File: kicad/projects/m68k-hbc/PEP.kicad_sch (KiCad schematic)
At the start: 10 parts, among them J1 PEP_Power_DIN41612_3x10, J12 PEP_Power_DIN41612_3x10, J13 PEP_Data_DIN41612_3x32, J2 PEP_Data_DIN41612_3x32, J5 PEP_Power_DIN41612_3x10, J8 PEP_Data_DIN41612_3x32, U13 74LS02, U23 MCP23017_SO

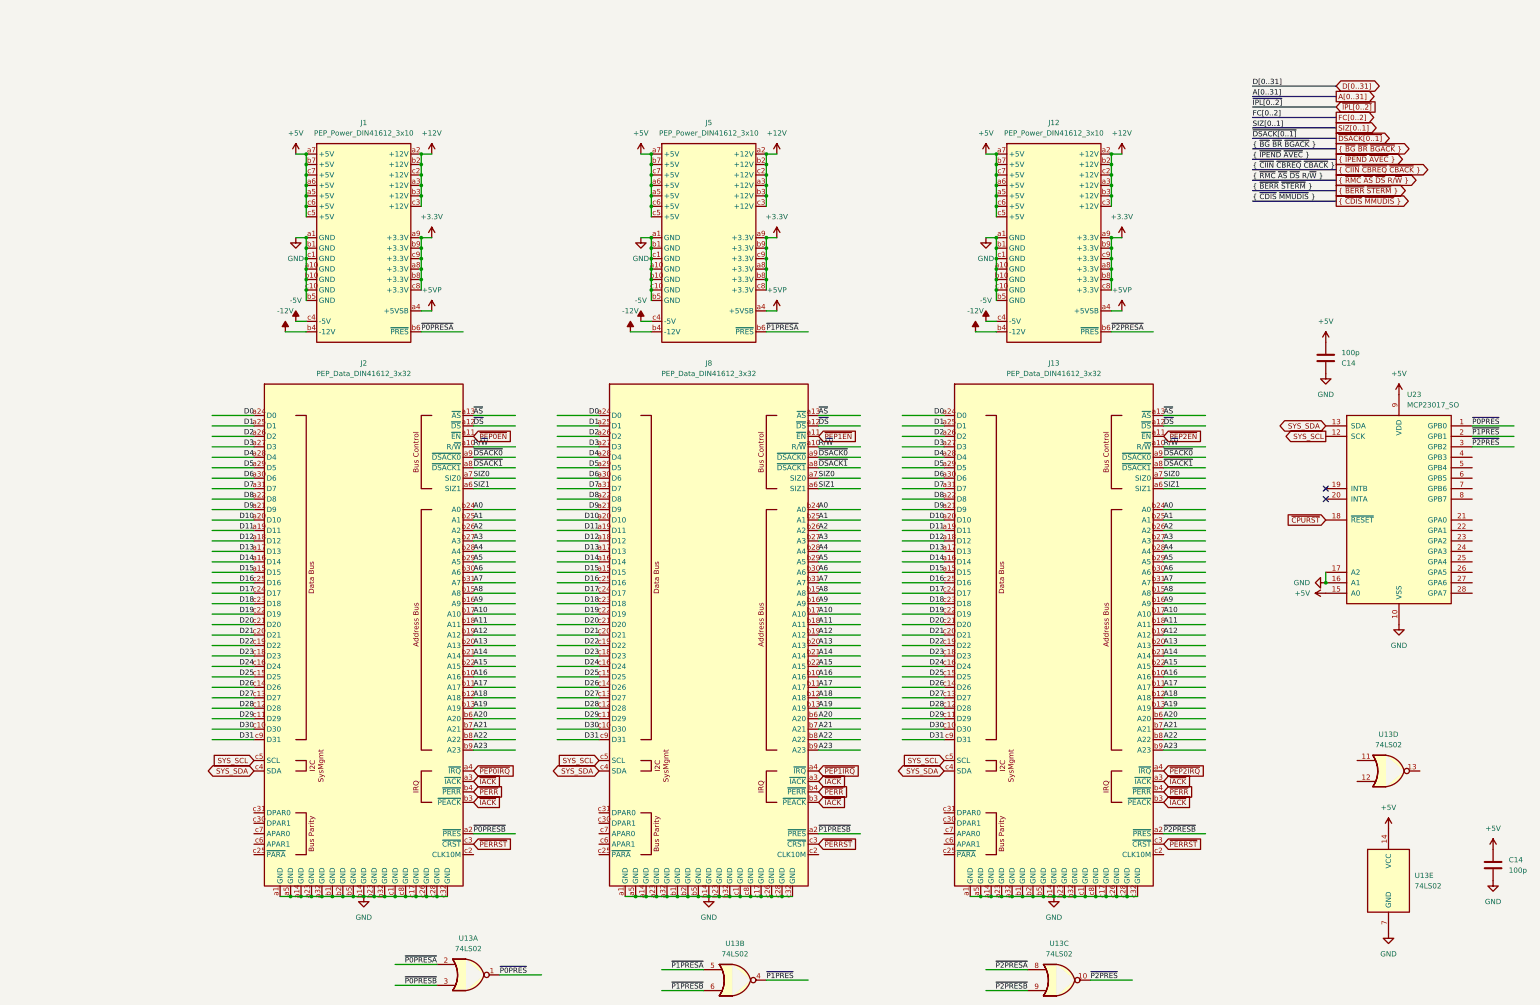
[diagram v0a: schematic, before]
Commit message: Modified system architecture, New KiCad Project: Cache Memory Module(SIMM80)
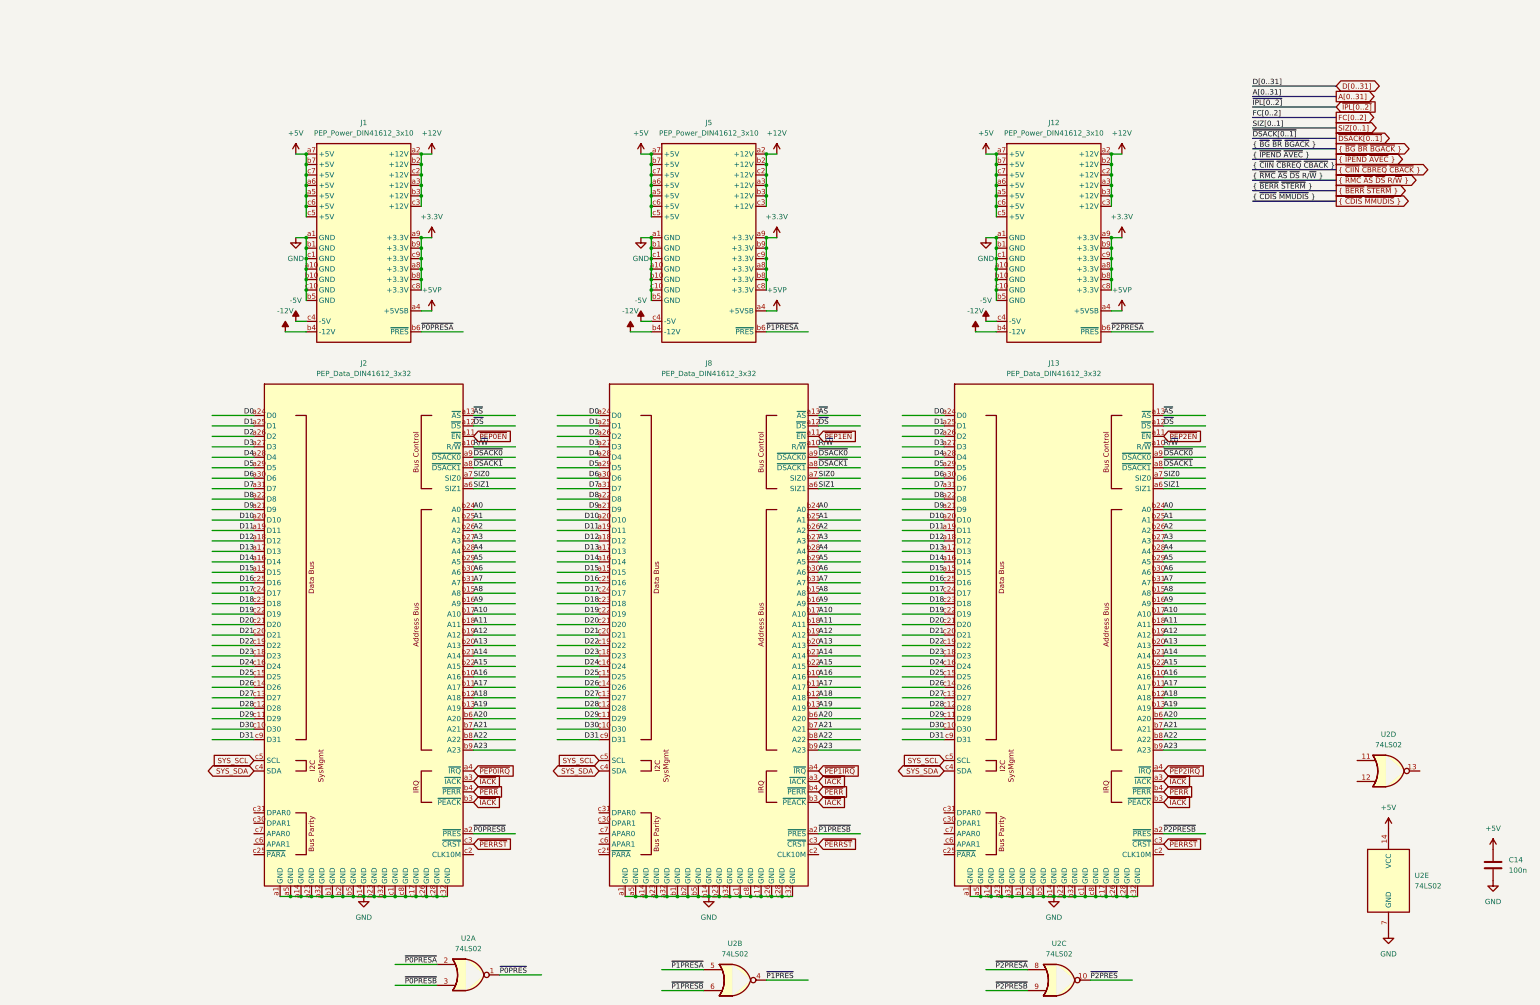
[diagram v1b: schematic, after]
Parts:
- removed C14: 100p, Capacitor_SMD:C_1206_3216Metric_Pad1.33x1.80mm_HandSolder, symbol Device:C
- removed U23: MCP23017_SO, Package_SO:SOIC-28W_7.5x17.9mm_P1.27mm, symbol Interface_Expansion:MCP23017_SO
- C14: value 100p -> 100n
- renumbered U13 to U2
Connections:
- no-connect marks 2 -> 0

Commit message: Some Updates
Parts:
- removed C14: 100n, Capacitor_SMD:C_1206_3216Metric_Pad1.33x1.80mm_HandSolder, symbol Device:C
- removed U2: 74LS02, Package_SO:SOIC-14W_7.5x9mm_P1.27mm, symbol 74xx:74LS02
- added RN1: 10k, Resistor_THT:R_Array_SIP8, symbol Device:R_Network07
- J13, J2, J8: symbol EPBus:PEP_Data_DIN41612_3x32 -> m68k-hbc-conn:PEP_Data_DIN41612_3x32
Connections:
- net A0 is gone; now on net GND: J13.b24 (GND), J2.b24 (GND), J8.b24 (GND)
- net A1 is gone; now on net GND: J13.b25 (GND), J2.b25 (GND), J8.b25 (GND)
- net A10 is gone; now on net GND: J13.b17 (GND), J2.b17 (GND), J8.b17 (GND)
- net A11 is gone; now on net GND: J13.b18 (GND), J2.b18 (GND), J8.b18 (GND)
- net A12 is gone; now on net GND: J13.b19 (GND), J2.b19 (GND), J8.b19 (GND)
- net A13 is gone; now on net GND: J13.b20 (GND), J2.b20 (GND), J8.b20 (GND)
- net A14 is gone; now on net GND: J13.b21 (GND), J2.b21 (GND), J8.b21 (GND)
- net A15 is gone; now on net GND: J13.b22 (GND), J2.b22 (GND), J8.b22 (GND)
- net A16 is gone; now on net GND: J13.b10 (GND), J2.b10 (GND), J8.b10 (GND)
- net A17 is gone; now on net GND: J13.b11 (GND), J2.b11 (GND), J8.b11 (GND)
- net A18 is gone; now on net GND: J13.b12 (GND), J2.b12 (GND), J8.b12 (GND)
- net A19 is gone; now on net GND: J13.b13 (GND), J2.b13 (GND), J8.b13 (GND)
- net A2 is gone; now on net GND: J13.b26 (GND), J2.b26 (GND), J8.b26 (GND)
- net A20 is gone; now on net GND: J13.b6 (GND), J2.b6 (GND), J8.b6 (GND)
- net A21 is gone; now on net GND: J13.b7 (GND), J2.b7 (GND), J8.b7 (GND)
- net A22 is gone; now on net GND: J13.b8 (GND), J2.b8 (GND), J8.b8 (GND)
- net A23 is gone; now on net GND: J13.b9 (GND), J2.b9 (GND), J8.b9 (GND)
- net A3 is gone; now on net GND: J13.b27 (GND), J2.b27 (GND), J8.b27 (GND)
- net A4 is gone; now on net GND: J13.b28 (GND), J2.b28 (GND), J8.b28 (GND)
- net A5 is gone; now on net GND: J13.b29 (GND), J2.b29 (GND), J8.b29 (GND)
- net A6 is gone; now on net GND: J13.b30 (GND), J2.b30 (GND), J8.b30 (GND)
- net A7 is gone; now on net GND: J13.b31 (GND), J2.b31 (GND), J8.b31 (GND)
- net A8 is gone; now on net GND: J13.b15 (GND), J2.b15 (GND), J8.b15 (GND)
- net A9 is gone; now on net GND: J13.b16 (GND), J2.b16 (GND), J8.b16 (GND)
- net D16 is gone; now on net GND: J13.c25 (GND), J2.c25 (GND), J8.c25 (GND)
- net ~{IACK} is gone; now on net GND: J13.a3 (GND), J13.b3 (GND), J2.a3 (GND), J2.b3 (GND), J8.a3 (GND), J8.b3 (GND)
- net ~{P0PRESB} is gone; now on net ~{PRES_P0}: J2.a2 (~{PRES})
- net ~{P1PRESB} is gone; now on net ~{PRES_P1}: J8.a2 (~{PRES})
- net ~{P2PRESB} is gone; now on net ~{PRES_P2}: J13.a2 (~{PRES})
- net ~{PEP1EN} is gone; now on net ~{MRDY}: J8.a11 (~{MRDY})
- net ~{PEP2EN} is gone; now on net ~{MRDY}: J13.a11 (~{MRDY})
- net +5V: now also RN1.1 (common)
- net GND: now also J13.b4 (GND), J13.c27 (GND), J13.c30 (GND), J13.c6 (GND), J13.c7 (GND), J2.b4 (GND), J2.c27 (GND), J2.c30 (GND), J2.c6 (GND), J2.c7 (GND), J8.b4 (GND), J8.c27 (GND), J8.c30 (GND), J8.c6 (GND), J8.c7 (GND); no longer J13.a5 (GND), J13.c28 (GND), J2.a5 (GND), J2.c28 (GND), J8.a5 (GND), J8.c28 (GND)
- net ~{PERR}: now also J13.c29 (~{PERR}), J2.c29 (~{PERR}), J8.c29 (~{PERR}), RN1.5 (R4); no longer J13.b4 (~{PERR}), J2.b4 (~{PERR}), J8.b4 (~{PERR})
- net CLK_PEP: now reaches J8.c2 (CLK)
- net CLK_PEP: now also J13.c2 (CLK), J2.c2 (CLK)
- net PARITY: now reaches J8.c31 (PAR)
- net PARITY: now also J13.c31 (PAR), J2.c31 (PAR)
- net D0 renamed AD7
- net D1 renamed AD6
- net D10 renamed AD10
- net D11 renamed AD11
- net D12 renamed AD12
- net D13 renamed AD13
- net D14 renamed AD14
- net D15 renamed AD15
- net D17 renamed AD17
- net D18 renamed AD18
- net D19 renamed AD19
- net D2 renamed AD5
- net D20 renamed AD20
- net D21 renamed AD21
- net D22 renamed AD22
- net D23 renamed AD23
- net D24 renamed AD24
- net D25 renamed AD25
- net D26 renamed AD26
- net D27 renamed AD27
- net D28 renamed AD28
- net D29 renamed AD29
- net D3 renamed AD4
- net D30 renamed AD30
- net D31 renamed AD31
- net D4 renamed AD3
- net D5 renamed AD2
- net D6 renamed AD1
- net D7 renamed AD0
- net D8 renamed AD8
- net D9 renamed AD9
- net R/~{W} renamed OP0
- net SIZ0 renamed OP3
- net SIZ1 renamed ~{INIT}
- net ~{INIT}: now also RN1.7 (R6)
- removed net ~{AS}: J13.a13 (~{AS}), J2.a13 (~{AS}), J8.a13 (~{AS})
- net ~{DSACK0} renamed OP1
- net ~{DSACK1} renamed OP2
- net ~{DS} renamed ~{CRDY}
- net ~{CRDY}: now also RN1.6 (R5)
- net ~{P0PRESA} renamed ~{PRES_P0}
- net ~{PRES_P0}: now also RN1.2 (R1)
- net ~{P1PRESA} renamed ~{PRES_P1}
- net ~{PRES_P1}: now also RN1.3 (R2)
- net ~{P2PRESA} renamed ~{PRES_P2}
- net ~{PRES_P2}: now also RN1.4 (R3)
- net ~{PEP0EN} renamed ~{MRDY}
- net ~{PEP0IRQ} renamed ~{IRQ_P0}
- net ~{PEP1IRQ} renamed ~{IRQ_P1}
- net ~{PEP2IRQ} renamed ~{IRQ_P2}
- net ~{PERRST} renamed ~{RST_PEP}
- new net AD16: J13.c25 (GND), J2.c25 (GND), J8.c25 (GND)
- new net ~{CERR_P0}: J2.c28 (~{CERR})
- new net ~{CERR_P1}: J8.c28 (~{CERR})
- new net ~{CERR_P2}: J13.c28 (~{CERR})
- new net ~{EN_P0}: J2.a13 (~{EN})
- new net ~{EN_P1}: J8.a13 (~{EN})
- new net ~{EN_P2}: J13.a13 (~{EN})
- new net ~{STOP}: J13.a5 (~{STOP}), J2.a5 (~{STOP}), J8.a5 (~{STOP}), RN1.8 (R7)
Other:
- note added: "PEP Signals"
- note added: "System Serial Bus"
- moved on the sheet: J1, J12, J5

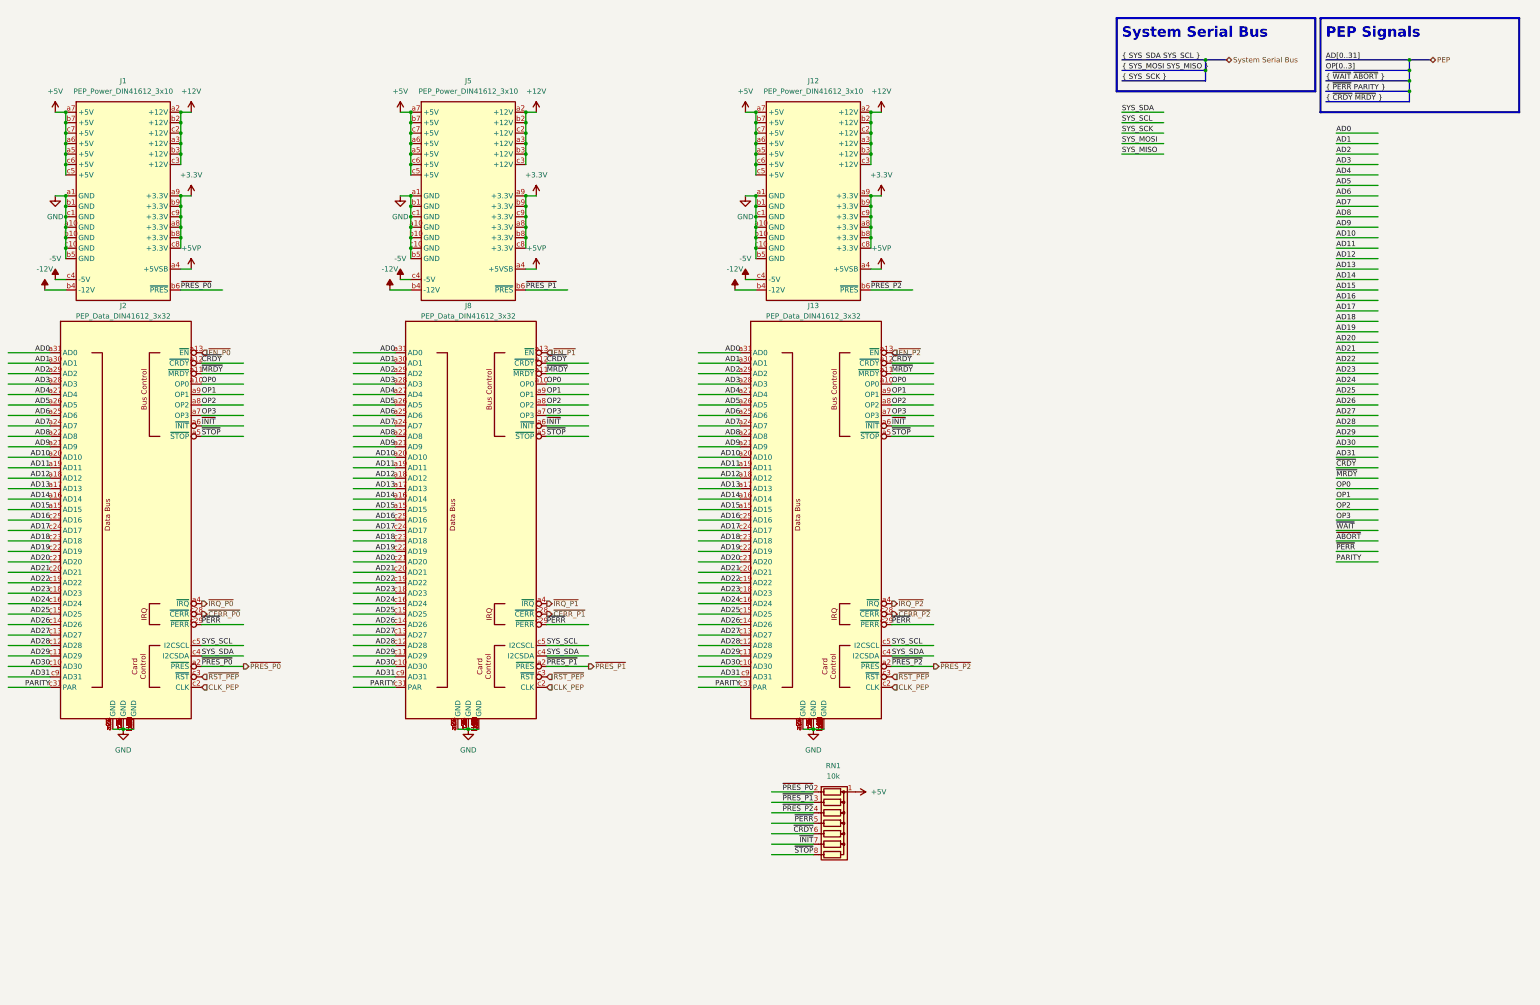
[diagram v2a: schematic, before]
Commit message: Large changes: EHBCSimpleEmu, kicad, fwcode, docs
This commit contains some large changes:
- Removed EHBCSimpleEmu (Moved to kms1212/llemu, kms1212/qemu)
- (likely) Removed fwcode; now it only boots and stops
- Modified documents
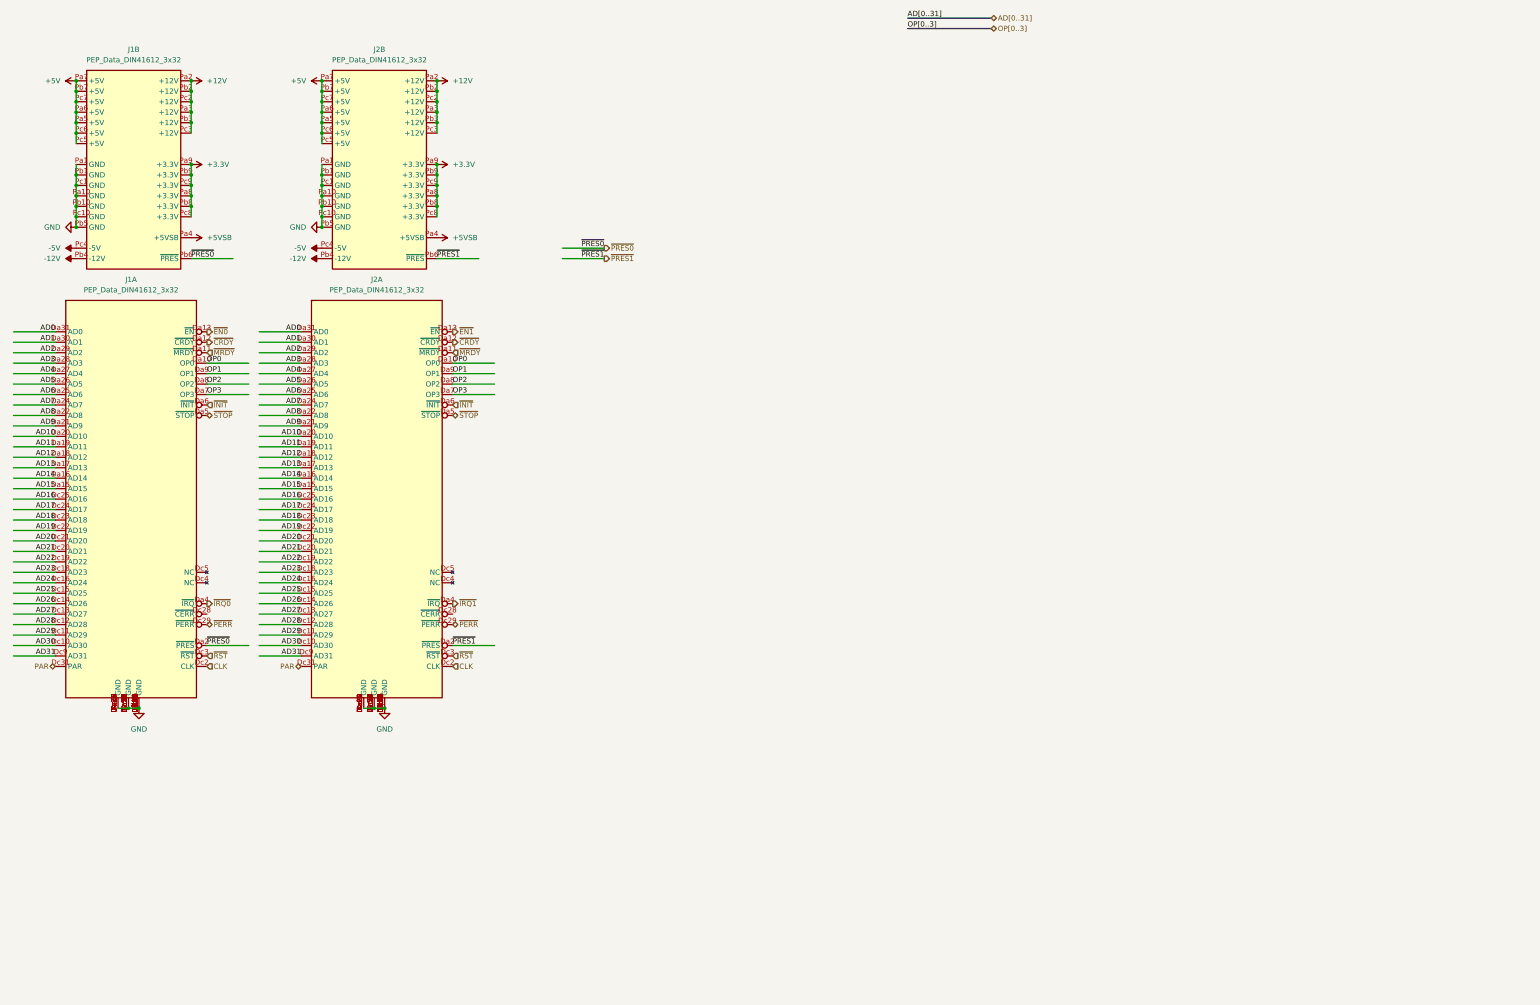
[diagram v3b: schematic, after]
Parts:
- removed J1, J12, J5: PEP_Power_DIN41612_3x10, Connector_DIN:DIN41612_C3_3x10_Female_Vertical_THT, symbol EPBus:PEP_Power_DIN41612_3x10
- removed J13, J2, J8: PEP_Data_DIN41612_3x32, Connector_DIN:DIN41612_C_3x32_Female_Vertical_THT, symbol m68k-hbc-conn:PEP_Data_DIN41612_3x32
- removed RN1: 10k, Resistor_THT:R_Array_SIP8, symbol Device:R_Network07
- added J1, J2: PEP_Data_DIN41612_3x32, m68k-hbc-conn:PEP_Board, symbol m68k-hbc-conn:PEP_Connector
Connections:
- net +12V: now also J1.Pa2 (+12V), J1.Pa3 (+12V), J1.Pb2 (+12V), J1.Pb3 (+12V), J1.Pc2 (+12V), J1.Pc3 (+12V), J2.Pa2 (+12V), J2.Pa3 (+12V), J2.Pb2 (+12V), J2.Pb3 (+12V), J2.Pc2 (+12V), J2.Pc3 (+12V)
- net +3.3V: now also J1.Pa8 (+3.3V), J1.Pa9 (+3.3V), J1.Pb8 (+3.3V), J1.Pb9 (+3.3V), J1.Pc8 (+3.3V), J1.Pc9 (+3.3V), J2.Pa8 (+3.3V), J2.Pa9 (+3.3V), J2.Pb8 (+3.3V), J2.Pb9 (+3.3V), J2.Pc8 (+3.3V), J2.Pc9 (+3.3V)
- net +5V: now also J1.Pa5 (+5V), J1.Pa6 (+5V), J1.Pa7 (+5V), J1.Pb7 (+5V), J1.Pc5 (+5V), J1.Pc6 (+5V), J1.Pc7 (+5V), J2.Pa5 (+5V), J2.Pa6 (+5V), J2.Pa7 (+5V), J2.Pb7 (+5V), J2.Pc5 (+5V), J2.Pc6 (+5V), J2.Pc7 (+5V)
- net -12V: now also J1.Pb4 (-12V), J2.Pb4 (-12V)
- net -5V: now also J1.Pc4 (-5V), J2.Pc4 (-5V)
- net AD0: now also J1.Da31 (AD0), J2.Da31 (AD0)
- net AD1: now also J1.Da30 (AD1), J2.Da30 (AD1)
- net AD10: now also J1.Da20 (AD10), J2.Da20 (AD10)
- net AD11: now also J1.Da19 (AD11), J2.Da19 (AD11)
- net AD12: now also J1.Da18 (AD12), J2.Da18 (AD12)
- net AD13: now also J1.Da17 (AD13), J2.Da17 (AD13)
- net AD14: now also J1.Da16 (AD14), J2.Da16 (AD14)
- net AD15: now also J1.Da15 (AD15), J2.Da15 (AD15)
- net AD16: now also J1.Dc25 (GND), J2.Dc25 (GND)
- net AD17: now also J1.Dc24 (AD17), J2.Dc24 (AD17)
- net AD18: now also J1.Dc23 (AD18), J2.Dc23 (AD18)
- net AD19: now also J1.Dc22 (AD19), J2.Dc22 (AD19)
- net AD2: now also J1.Da29 (AD2), J2.Da29 (AD2)
- net AD20: now also J1.Dc21 (AD20), J2.Dc21 (AD20)
- net AD21: now also J1.Dc20 (AD21), J2.Dc20 (AD21)
- net AD22: now also J1.Dc19 (AD22), J2.Dc19 (AD22)
- net AD23: now also J1.Dc18 (AD23), J2.Dc18 (AD23)
- net AD24: now also J1.Dc16 (AD24), J2.Dc16 (AD24)
- net AD25: now also J1.Dc15 (AD25), J2.Dc15 (AD25)
- net AD26: now also J1.Dc14 (AD26), J2.Dc14 (AD26)
- net AD27: now also J1.Dc13 (AD27), J2.Dc13 (AD27)
- net AD28: now also J1.Dc12 (AD28), J2.Dc12 (AD28)
- net AD29: now also J1.Dc11 (AD29), J2.Dc11 (AD29)
- net AD3: now also J1.Da28 (AD3), J2.Da28 (AD3)
- net AD30: now also J1.Dc10 (AD30), J2.Dc10 (AD30)
- net AD31: now also J1.Dc9 (AD31), J2.Dc9 (AD31)
- net AD4: now also J1.Da27 (AD4), J2.Da27 (AD4)
- net AD5: now also J1.Da26 (AD5), J2.Da26 (AD5)
- net AD6: now also J1.Da25 (AD6), J2.Da25 (AD6)
- net AD7: now also J1.Da24 (AD7), J2.Da24 (AD7)
- net AD8: now also J1.Da22 (AD8), J2.Da22 (AD8)
- net AD9: now also J1.Da21 (AD9), J2.Da21 (AD9)
- net GND: now also J1.Da1 (GND), J1.Da14 (GND), J1.Da23 (GND), J1.Da3 (GND), J1.Da32 (GND), J1.Db1 (GND), J1.Db10 (GND), J1.Db11 (GND), J1.Db12 (GND), J1.Db13 (GND), J1.Db14 (GND), J1.Db15 (GND), J1.Db16 (GND), J1.Db17 (GND), J1.Db18 (GND), J1.Db19 (GND), J1.Db2 (GND), J1.Db20 (GND), J1.Db21 (GND), J1.Db22 (GND), J1.Db23 (GND), J1.Db24 (GND), J1.Db25 (GND), J1.Db26 (GND), J1.Db27 (GND), J1.Db28 (GND), J1.Db29 (GND), J1.Db3 (GND), J1.Db30 (GND), J1.Db31 (GND), J1.Db32 (GND), J1.Db4 (GND), J1.Db5 (GND), J1.Db6 (GND), J1.Db7 (GND), J1.Db8 (GND), J1.Db9 (GND), J1.Dc1 (GND), J1.Dc17 (GND), J1.Dc25 (GND), J1.Dc26 (GND), J1.Dc27 (GND), J1.Dc30 (GND), J1.Dc32 (GND), J1.Dc6 (GND), J1.Dc7 (GND), J1.Dc8 (GND), J1.Pa1 (GND), J1.Pa10 (GND), J1.Pb1 (GND), J1.Pb10 (GND), J1.Pb5 (GND), J1.Pc1 (GND), J1.Pc10 (GND), J2.Da1 (GND), J2.Da14 (GND), J2.Da23 (GND), J2.Da3 (GND), J2.Da32 (GND), J2.Db1 (GND), J2.Db10 (GND), J2.Db11 (GND), J2.Db12 (GND), J2.Db13 (GND), J2.Db14 (GND), J2.Db15 (GND), J2.Db16 (GND), J2.Db17 (GND), J2.Db18 (GND), J2.Db19 (GND), J2.Db2 (GND), J2.Db20 (GND), J2.Db21 (GND), J2.Db22 (GND), J2.Db23 (GND), J2.Db24 (GND), J2.Db25 (GND), J2.Db26 (GND), J2.Db27 (GND), J2.Db28 (GND), J2.Db29 (GND), J2.Db3 (GND), J2.Db30 (GND), J2.Db31 (GND), J2.Db32 (GND), J2.Db4 (GND), J2.Db5 (GND), J2.Db6 (GND), J2.Db7 (GND), J2.Db8 (GND), J2.Db9 (GND), J2.Dc1 (GND), J2.Dc17 (GND), J2.Dc25 (GND), J2.Dc26 (GND), J2.Dc27 (GND), J2.Dc30 (GND), J2.Dc32 (GND), J2.Dc6 (GND), J2.Dc7 (GND), J2.Dc8 (GND), J2.Pa1 (GND), J2.Pa10 (GND), J2.Pb1 (GND), J2.Pb10 (GND), J2.Pb5 (GND), J2.Pc1 (GND), J2.Pc10 (GND)
- net OP0: now also J1.Da10 (OP0), J2.Da10 (OP0)
- net OP1: now also J1.Da9 (OP1), J2.Da9 (OP1)
- net OP2: now also J1.Da8 (OP2), J2.Da8 (OP2)
- net OP3: now also J1.Da7 (OP3), J2.Da7 (OP3)
- net ~{CRDY}: now also J1.Da12 (~{CRDY}), J2.Da12 (~{CRDY})
- net ~{INIT}: now also J1.Da6 (~{INIT}), J2.Da6 (~{INIT})
- net ~{MRDY}: now also J1.Da11 (~{MRDY}), J2.Da11 (~{MRDY})
- net ~{PERR}: now also J1.Dc29 (~{PERR}), J2.Dc29 (~{PERR})
- net ~{STOP}: now also J1.Da5 (~{STOP}), J2.Da5 (~{STOP})
- new net +5VSB: J1.Pa4 (+5VSB), J2.Pa4 (+5VSB)
- new net CLK: J1.Dc2 (CLK), J2.Dc2 (CLK)
- new net PAR: J1.Dc31 (PAR), J2.Dc31 (PAR)
- new net ~{EN0}: J1.Da13 (~{EN})
- new net ~{EN1}: J2.Da13 (~{EN})
- new net ~{IRQ0}: J1.Da4 (~{IRQ})
- new net ~{IRQ1}: J2.Da4 (~{IRQ})
- new net ~{PRES0}: J1.Da2 (~{PRES}), J1.Pb6 (~{PRES})
- new net ~{PRES1}: J2.Da2 (~{PRES}), J2.Pb6 (~{PRES})
- new net ~{RST}: J1.Dc3 (~{RST}), J2.Dc3 (~{RST})
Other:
- note removed: "PEP Signals"
- note removed: "System Serial Bus"
